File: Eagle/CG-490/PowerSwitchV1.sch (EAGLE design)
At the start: 24 parts, among them IC1 LM393D, Q1 2N3906, T1 SFH 309

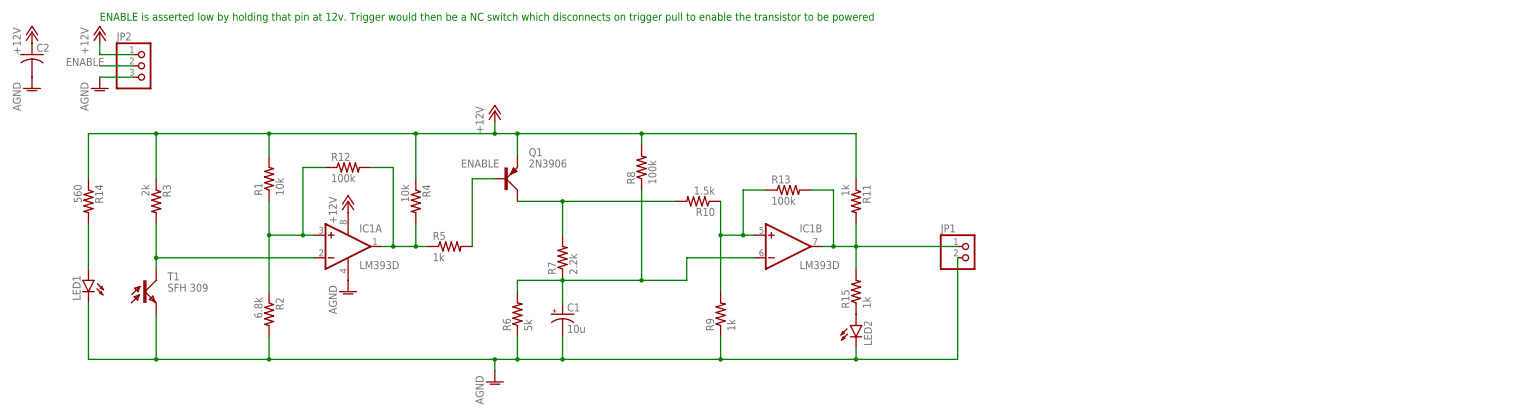
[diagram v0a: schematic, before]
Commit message: layout for optical trigger and complete circuit underway
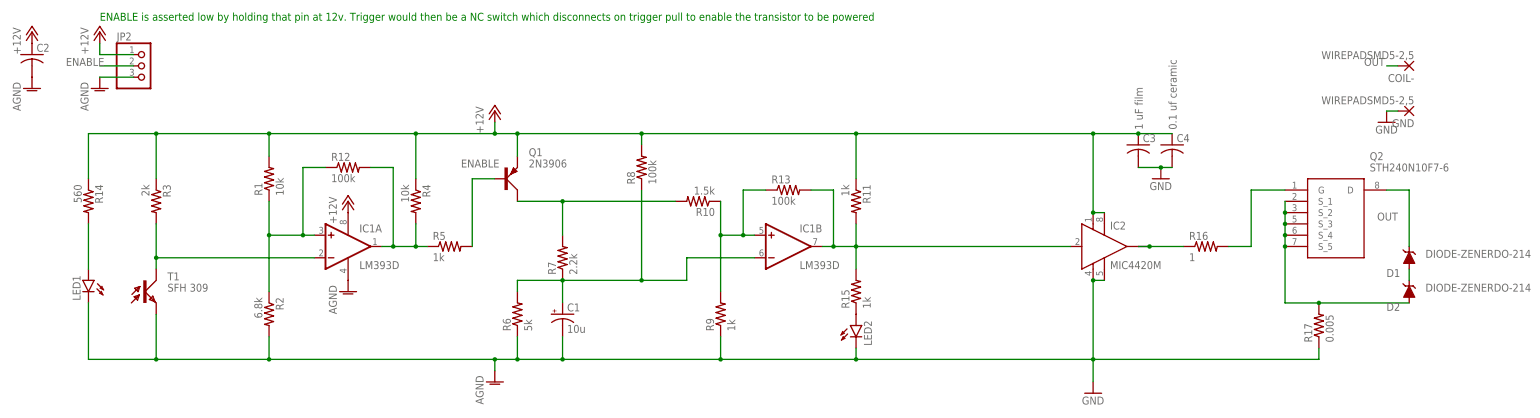
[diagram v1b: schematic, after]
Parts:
- removed JP1: (no value), pinhead:PINHD-1X2
- added C3: 1 uF film, rcl:C-US050-045X075
- added C4: 0.1 uf ceramic, rcl:C-US025-030X050
- added COIL-, GND: WIREPADSMD5-2,5, wirepad:WIREPADSMD5-2,5
- added D1, D2: DIODE-ZENERDO-214, sparkfun-discretesemi:DIODE-ZENERDO-214
- added IC2: MIC4420M, transistor-power:MIC4420M
- added Q2: STH240N10F7-6, STH240N10F7-6:STH240N10F7-6
- added R16: 1, rcl:R-US_0207/7
- added R17: 0.005, rcl:R-US_R1206
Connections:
- new net GND: C3.2, C4.2, GND.P
- new net N$10: D1.A, D2.C
- new net N$14: D2.A, Q2.S_1, Q2.S_2, Q2.S_3, Q2.S_4, Q2.S_5, R17.2
- new net N$15: Q2.G, R16.2
- new net N$4: IC2.OUT@1, IC2.OUT@2, R16.1
- new net OUT: COIL-.P, D1.C, Q2.D
- net +12V: now also C3.1, C4.1, IC2.VS, IC2.VS1
- net AGND: now also IC2.GND, IC2.GND1, R17.1; no longer JP1.2
- net N$13: now also IC2.IN; no longer JP1.1

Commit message: updated board layouts
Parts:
- removed COIL-, GND: WIREPADSMD5-2,5, wirepad:WIREPADSMD5-2,5
- R15: value 1k -> 0.005; device rcl:R-US_R0603 -> rcl:R-US_R1206
- R16: value 1 -> 2; device rcl:R-US_0207/7 -> rcl:R-US_M0805
- renumbered LED1 to TRIG_LED, T1 to TRIG-TRANS
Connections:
- removed net N$2: LED2.A, R15.1
- net AGND: now also R15.1
- net GND: no longer GND.P
- net N$13: now also LED2.A; no longer R15.2
- net N$14: now also R15.2
- net OUT: no longer COIL-.P
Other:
- moved on the sheet: R15

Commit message: finalized schematic/pcb, updated report
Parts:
- added C_SENSE: (no value), pinhead:PINHD-1X2
- added TRIG: (no value), pinhead:PINHD-1X3
- added TRIG_SEL: (no value), jumper:SJ
- renumbered TRIG-TRANS to RX, TRIG_LED to TX
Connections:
- removed net GND: C3.2, C4.2
- new net N$2: IC2.IN, TRIG.1, TRIG_SEL.2
- net AGND: now also C3.2, C4.2, C_SENSE.1, TRIG.3
- net N$13: now also TRIG.2, TRIG_SEL.1; no longer IC2.IN
- net N$14: now also C_SENSE.2
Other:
- note removed: "ENABLE is asserted low by holding that pin at 12v. Trigger would then be a NC switch which disconnects on trigger pull to enable the transistor to be powered"
